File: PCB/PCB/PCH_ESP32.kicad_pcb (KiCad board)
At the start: 2 copper layers, 85 x 59.5 mm, 22 parts, among them J1 Conn_01x16_Pin, J2 Conn_01x16_Pin

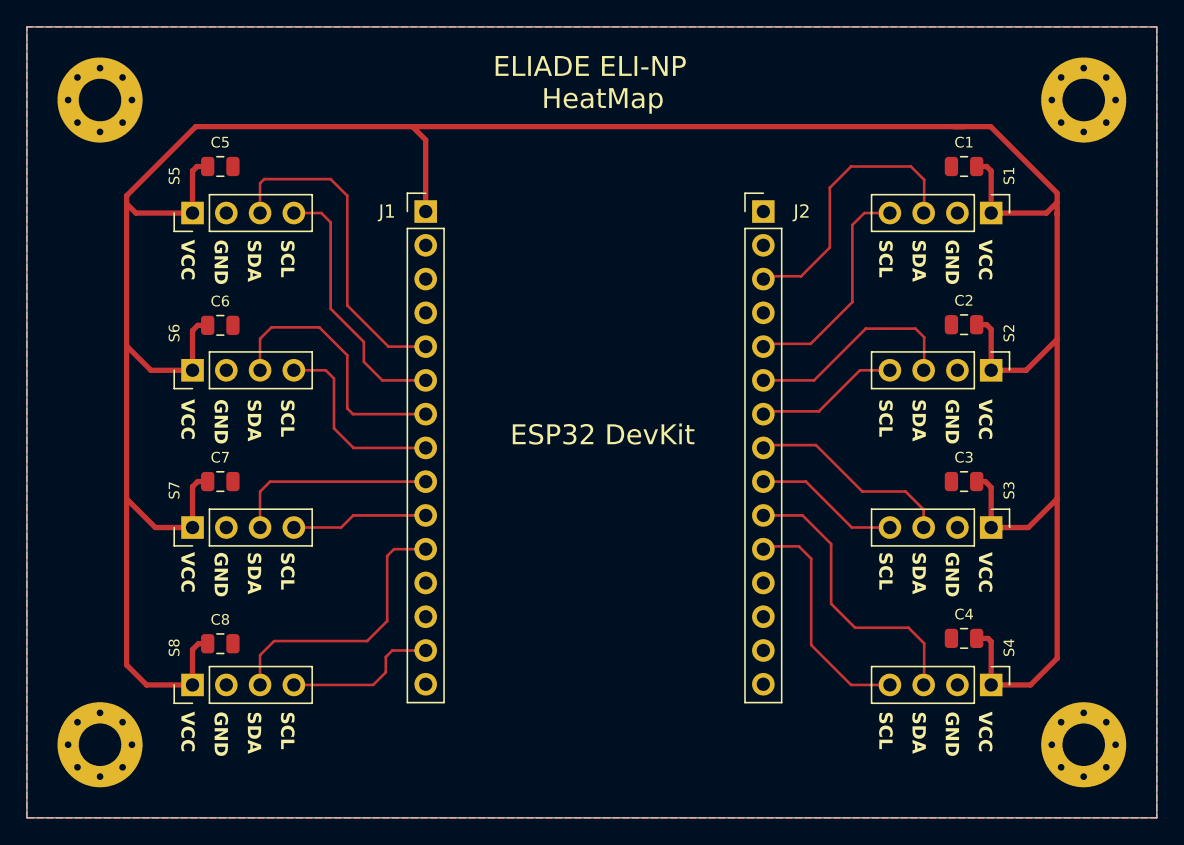
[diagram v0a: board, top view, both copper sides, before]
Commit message: added the new pcb design, and fixel the code to write real values
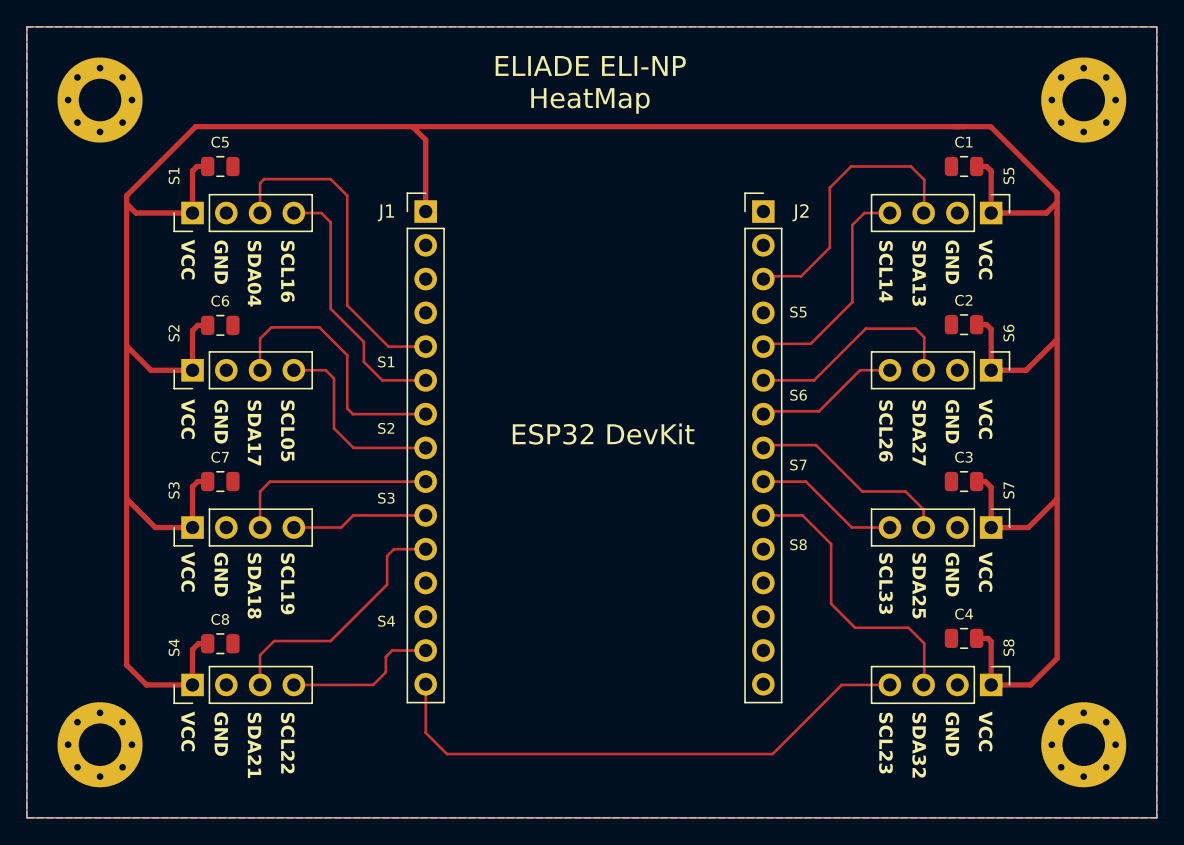
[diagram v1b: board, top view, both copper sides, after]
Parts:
- renumbered S5 to S1, S6 to S2, S7 to S3, S8 to S4, S1 to S5, S2 to S6, S3 to S7, S4 to S8
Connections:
- J1 pad 15: unconnected-(J1-Pin_15-Pad15) -> Net-(J1-Pin_15)
- J2 pad 11: Net-(J2-Pin_11) -> unconnected-(J2-Pin_11-Pad11)
- S8 pad 4: Net-(J2-Pin_11) -> Net-(J1-Pin_15)
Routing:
- net Net-(J1-Pin_15): track 0.00 -> 41.4 mm
- net Net-(J2-Pin_11): track 17.6 -> 0.00 mm
- net Net-(J1-Pin_11): track 20.9 -> 19.3 mm
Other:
- board text added: "S1"
- board text added: "S2"
- board text added: "S3"
- board text added: "S4"
- board text added: "S5"
- board text added: "S6"
- board text added: "S7"
- board text added: "S8"
- board text added: "SCL05"
- board text added: "SCL14"
- board text added: "SCL16"
- board text added: "SCL19"
- board text added: "SCL22"
- board text added: "SCL23"
- board text added: "SCL26"
- board text added: "SCL33"
- board text added: "SDA04"
- board text added: "SDA13"
- board text added: "SDA17"
- board text added: "SDA18"
- board text added: "SDA21"
- board text added: "SDA25"
- board text added: "SDA27"
- board text added: "SDA32"
- board text removed: "SCL"
- board text removed: "SDA"
